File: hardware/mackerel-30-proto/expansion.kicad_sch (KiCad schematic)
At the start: 0 parts

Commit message: rough layout of the PCB components
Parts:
- added J14: DIN41612_03x32_ABC, Connector_DIN:DIN41612_C_3x32_Female_Vertical_THT, symbol mackerel-68k-symbols:DIN41612_03x32_ABC
- added U14, U15, U16, U17, U18, U19, U20: 74HC245, Package_DIP:DIP-20_W7.62mm_Socket, symbol 74xx:74HC245
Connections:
- new net GND: J14.b1 (Pin_b1), J14.b10 (Pin_b10), J14.b11 (Pin_b11), J14.b12 (Pin_b12), J14.b13 (Pin_b13), J14.b14 (Pin_b14), J14.b15 (Pin_b15), J14.b16 (Pin_b16), J14.b17 (Pin_b17), J14.b18 (Pin_b18), J14.b19 (Pin_b19), J14.b2 (Pin_b2), J14.b20 (Pin_b20), J14.b21 (Pin_b21), J14.b22 (Pin_b22), J14.b23 (Pin_b23), J14.b24 (Pin_b24), J14.b25 (Pin_b25), J14.b26 (Pin_b26), J14.b27 (Pin_b27), J14.b28 (Pin_b28), J14.b29 (Pin_b29), J14.b3 (Pin_b3), J14.b30 (Pin_b30), J14.b31 (Pin_b31), J14.b32 (Pin_b32), J14.b4 (Pin_b4), J14.b5 (Pin_b5), J14.b6 (Pin_b6), J14.b7 (Pin_b7), J14.b8 (Pin_b8), J14.b9 (Pin_b9)
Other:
- note added: "16-bit Data Bus"
- note added: "24-bit address bus"
- note added: "Buffered inputs"
- note added: "Buffered outputs"
- note added: "TODO: 16 bit capable expansion bus, buffered"

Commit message: Routed power supply section
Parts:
- renumbered U19 to U14, U16 to U15, U18 to U16, U14 to U17, U15 to U18, U17 to U19
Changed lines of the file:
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@@
 		(dnp no)
 		(fields_autoplaced yes)
-		(property "Reference" "U18"
+		(property "Reference" "U16"
 			(at 41.5641 140.97 0)
 			(effects
@@
 			(project "mackerel-30-proto"
 				(path "/9307474f-ec99-494d-b4c9-fbd0b10ce86a/58e55b71-9977-4edb-8de3-43aa6ee7fcfc"
-					(reference "U18")
+					(reference "U16")
 					(unit 1)
 				)
@@
 		(dnp no)
 		(fields_autoplaced yes)
-		(property "Reference" "U14"
+		(property "Reference" "U17"
 			(at 42.8341 25.4 0)
 			(effects
@@
 			(project "mackerel-30-proto"
 				(path "/9307474f-ec99-494d-b4c9-fbd0b10ce86a/58e55b71-9977-4edb-8de3-43aa6ee7fcfc"
-					(reference "U14")
+					(reference "U17")
 					(unit 1)
 				)
@@
 		(dnp no)
 		(fields_autoplaced yes)
-		(property "Reference" "#PWR090"
+		(property "Reference" "#PWR088"
 			(at 214.63 132.08 0)
 			(effects
@@
 			(project ""
 				(path "/9307474f-ec99-494d-b4c9-fbd0b10ce86a/58e55b71-9977-4edb-8de3-43aa6ee7fcfc"
-					(reference "#PWR090")
+					(reference "#PWR088")
 					(unit 1)
 				)
@@
 		(dnp no)
 		(fields_autoplaced yes)
-		(property "Reference" "U16"
+		(property "Reference" "U15"
 			(at 41.5641 88.9 0)
 			(effects
@@
 			(project "mackerel-30-proto"
 				(path "/9307474f-ec99-494d-b4c9-fbd0b10ce86a/58e55b71-9977-4edb-8de3-43aa6ee7fcfc"
-					(reference "U16")
+					(reference "U15")
 					(unit 1)
 				)
@@
 		(dnp no)
 		(fields_autoplaced yes)
-		(property "Reference" "U15"
+		(property "Reference" "U18"
 			(at 75.8541 25.4 0)
 			(effects
@@
 			(project "mackerel-30-proto"
 				(path "/9307474f-ec99-494d-b4c9-fbd0b10ce86a/58e55b71-9977-4edb-8de3-43aa6ee7fcfc"
-					(reference "U15")
+					(reference "U18")
 					(unit 1)
 				)
@@
 		(dnp no)
 		(fields_autoplaced yes)
-		(property "Reference" "U17"
+		(property "Reference" "U19"
 			(at 77.1241 87.63 0)
 			(effects
@@
 			(project "mackerel-30-proto"
 				(path "/9307474f-ec99-494d-b4c9-fbd0b10ce86a/58e55b71-9977-4edb-8de3-43aa6ee7fcfc"
-					(reference "U17")
+					(reference "U19")
 					(unit 1)
 				)
@@
 		(dnp no)
 		(fields_autoplaced yes)
-		(property "Reference" "U19"
+		(property "Reference" "U14"
 			(at 3.4641 92.71 0)
 			(effects
@@
 			(project "mackerel-30-proto"
 				(path "/9307474f-ec99-494d-b4c9-fbd0b10ce86a/58e55b71-9977-4edb-8de3-43aa6ee7fcfc"
-					(reference "U19")
+					(reference "U14")
 					(unit 1)
 				)

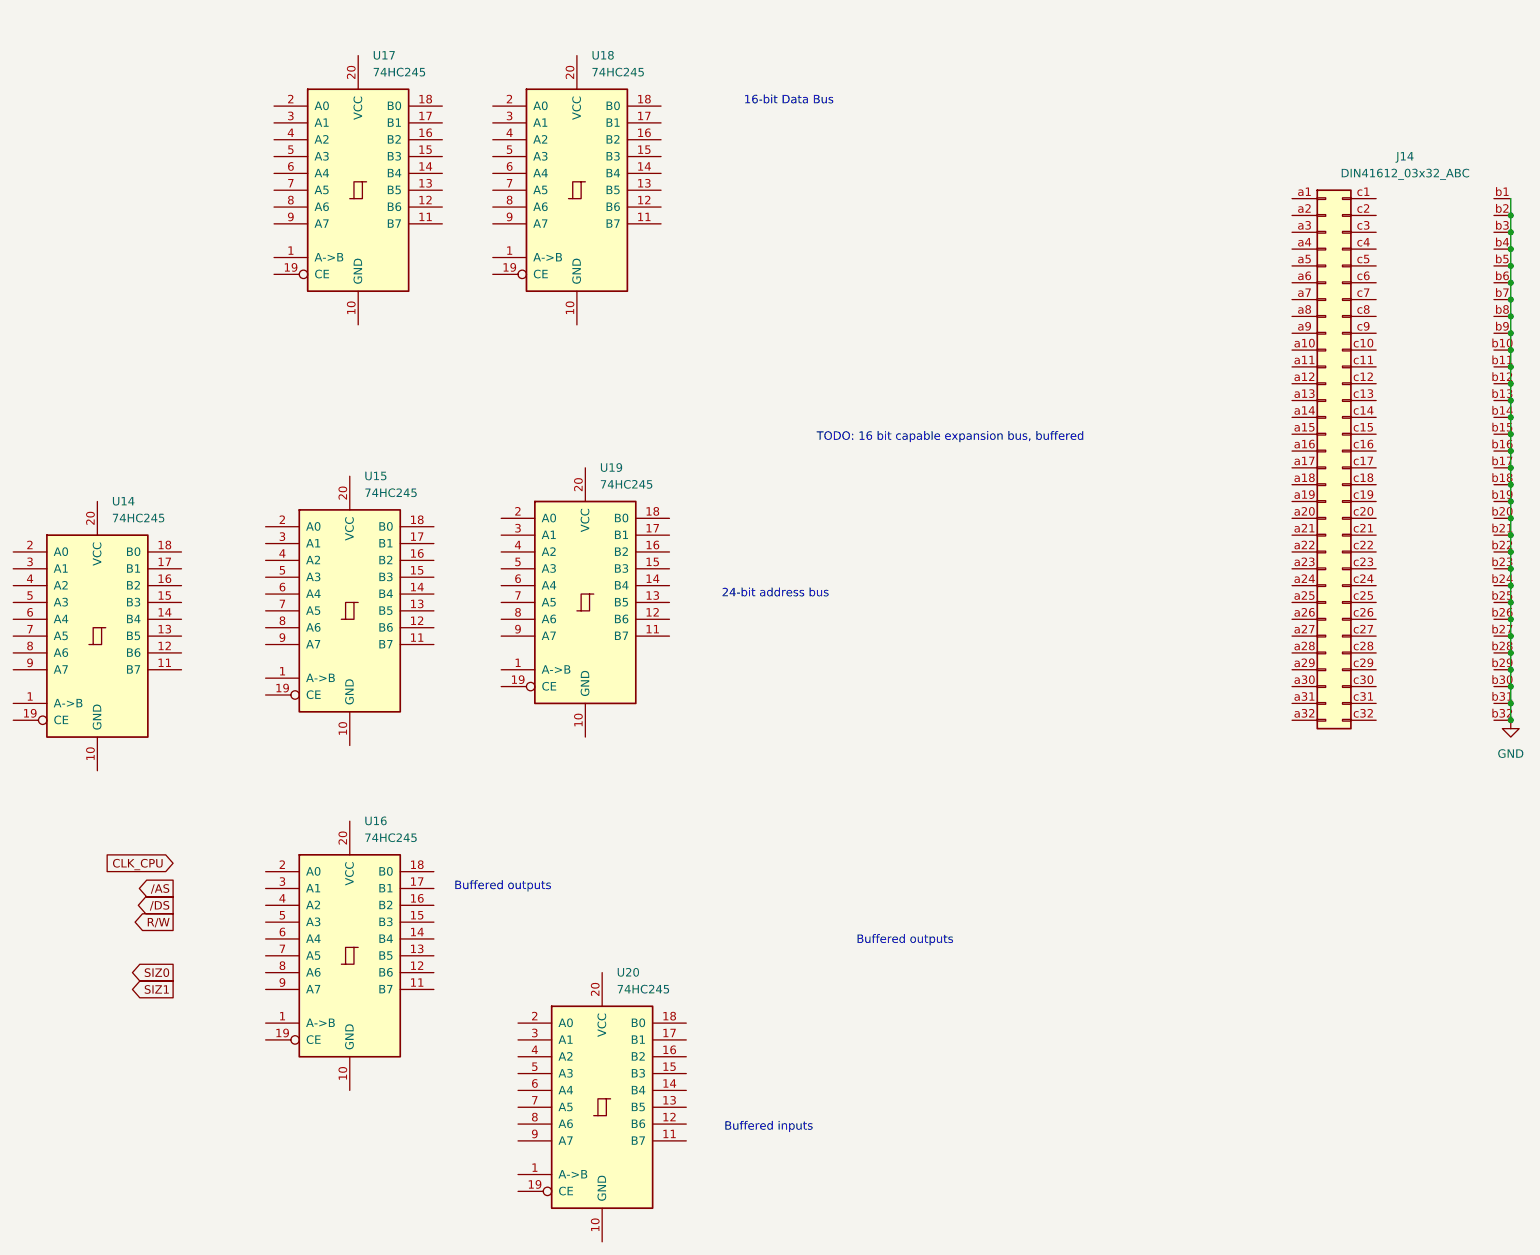
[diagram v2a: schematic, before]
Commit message: Routed ROM and SRAM
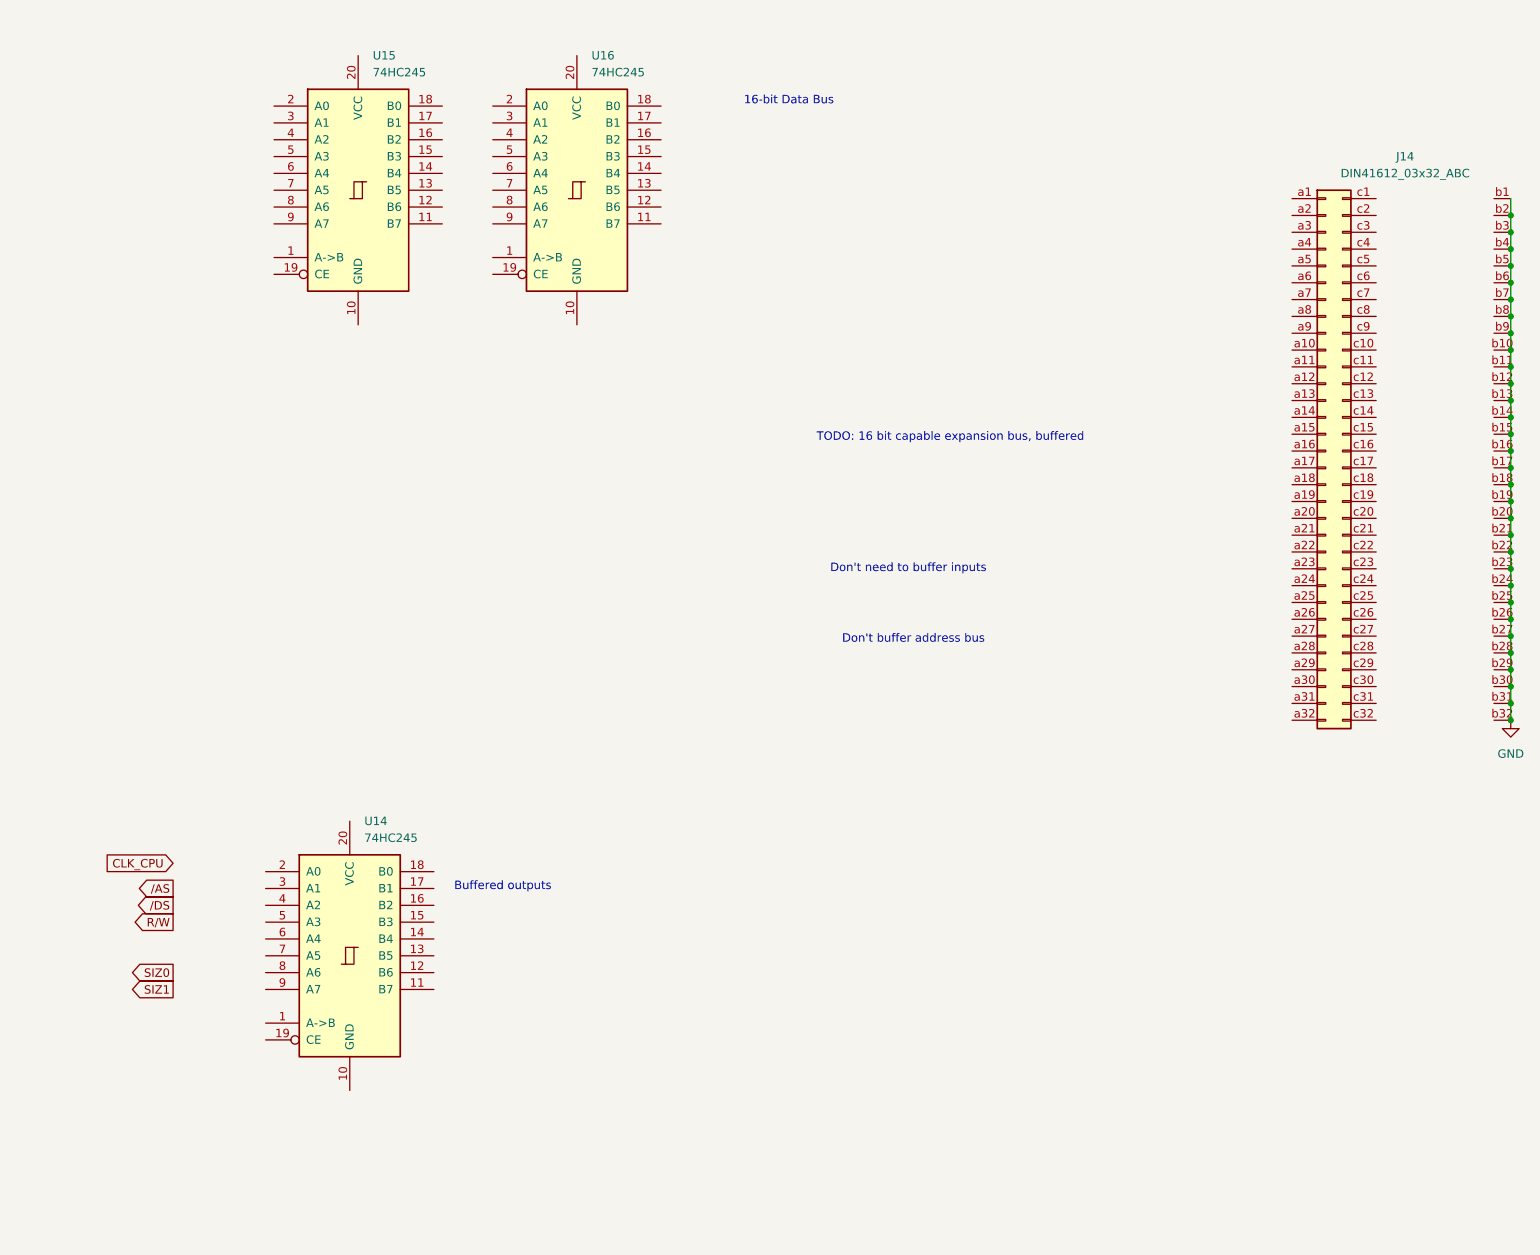
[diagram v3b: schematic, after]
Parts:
- removed U14, U15, U19, U20: 74HC245, Package_DIP:DIP-20_W7.62mm_Socket, symbol 74xx:74HC245
- renumbered U16 to U14, U17 to U15, U18 to U16
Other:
- note added: "Don't buffer address bus"
- note added: "Don't need to buffer inputs"
- note removed: "24-bit address bus"
- note removed: "Buffered inputs"
